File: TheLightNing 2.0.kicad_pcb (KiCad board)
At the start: 2 copper layers, 71 x 51 mm, 26 parts, among them J1 motores izq, J2 motores der, J3 batt, J4 LED_izq, SW1 SW_SPDT, U1 L298(H)N, U2 ESP32_DEVKITC, U3 L7805

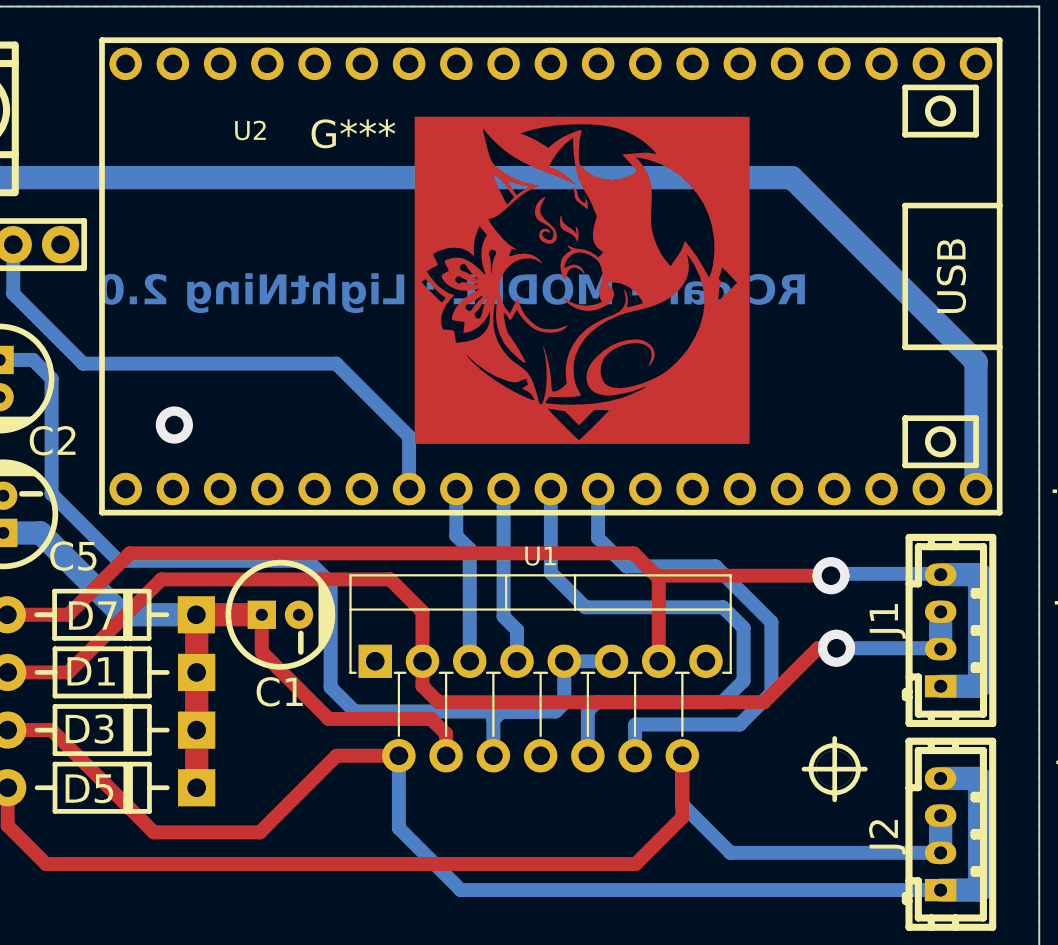
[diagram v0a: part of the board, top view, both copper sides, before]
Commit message: buzzer agregado
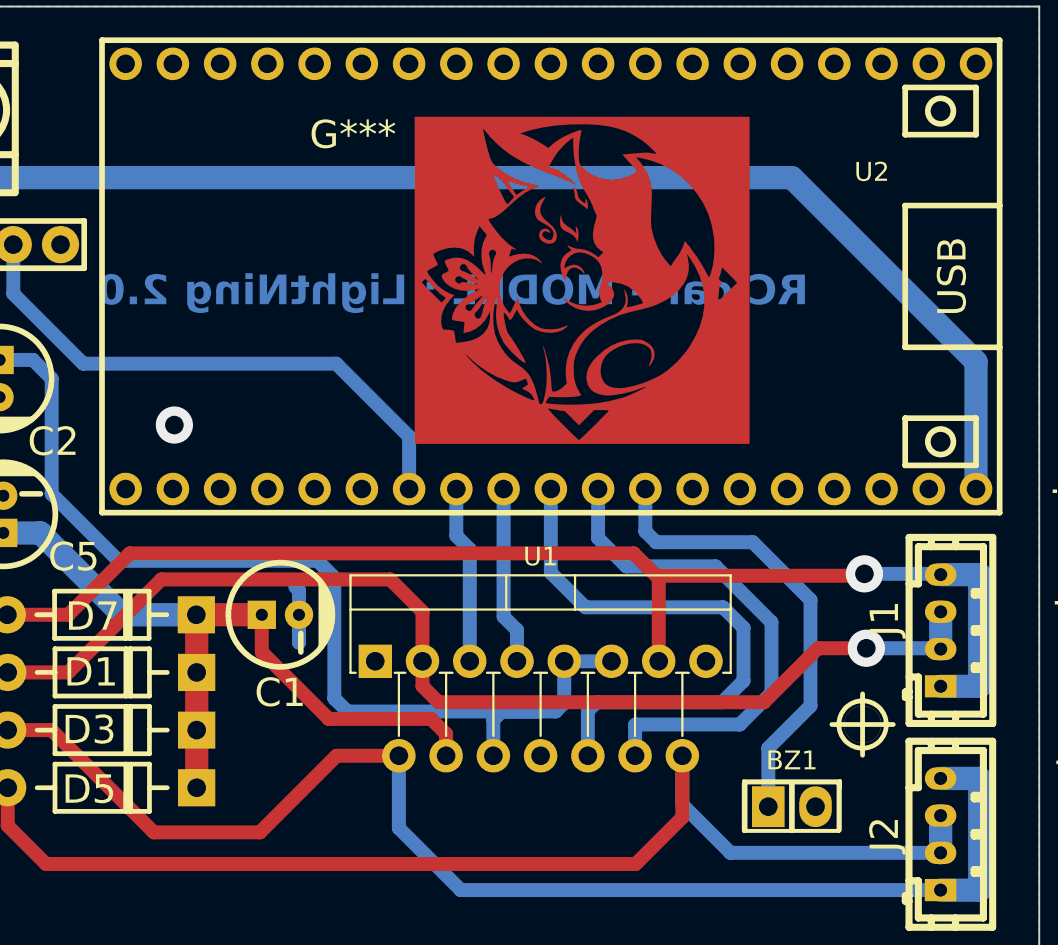
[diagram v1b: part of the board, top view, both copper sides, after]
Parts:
- added BZ1: Buzzer, EESTN5:Pin_Header_2, F.Cu at (92.7, 71.7)
- moved hole_2mm 2.83 mm to (96.5, 67.6)
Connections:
- U2 pad 12: unconnected-(U2-IO14-Pad12) -> /buzz
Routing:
- net /buzz: track 0.00 -> 24.7 mm
- net GND: track 0.00 -> 4.58 mm
- net +5V: track 142.8 -> 143.3 mm

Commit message: re-made
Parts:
- removed G***: LOGO, logo:yae
- removed H1: salida, EESTN5:hole_1mm
- removed the hole_2mm at (96.5, 67.6)
- removed the hole_2mm at (37.0, 77.0)
- removed the hole_2mm at (37.0, 31.0)
- added C6: 100uF 25v, EESTN5:CAP_ELEC_5x11mm, F.Cu at (119.6, 90.4)
- added D9: LED, EESTN5:Pin_strip_2, F.Cu at (120.0, 83.1)
- added J5: dc jack, EESTN5:Pin_Strip_3, F.Cu at (171.1, 97.3)
- added R1: 330, EESTN5:RES0.3, F.Cu at (124.5, 86.9)
- added R2: 22 2W, EESTN5:RES0.3, F.Cu at (127.5, 86.9)
- added U4: L7805, EESTN5:TO-220, F.Cu at (113.8, 88.9)
- added hole_2mm: VAL**, EESTN5:hole_2mm, F.Cu at (187.5, 97.5)
- added hole_2mm: VAL**, EESTN5:hole_2mm, F.Cu at (112.5, 97.5)
- added hole_2mm: VAL**, EESTN5:hole_2mm, F.Cu at (112.5, 42.5)
- moved D4 141.7 mm to (181.3, 42.4), turned to 180 degrees
- moved D6 141.7 mm to (181.3, 45.5), turned to 180 degrees
- moved D8 140.0 mm to (181.3, 48.6), turned to 180 degrees
- moved D2 140.0 mm to (181.3, 51.7), turned to 180 degrees
- moved C1 122.8 mm to (184.9, 89.0)
- moved D3 114.8 mm to (167.6, 42.4), turned to 180 degrees
- moved D5 114.8 mm to (167.6, 45.5), turned to 180 degrees
- moved D7 112.8 mm to (167.6, 48.6), turned to 180 degrees
- moved D1 112.7 mm to (167.6, 51.7), turned to 180 degrees
- moved U1 99.5 mm to (168.5, 80.1), turned to 90 degrees
- moved SW1 82.1 mm to (115.6, 75.0)
- moved J4 80.9 mm to (124.6, 75.0), turned to 90 degrees
- moved J2 77.5 mm to (176.1, 91.2), turned to 0 degrees
- moved J3 76.6 mm to (115.6, 66.5), turned to 90 degrees
- moved C3 75.8 mm to (119.9, 55.6)
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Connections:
- SW1 pad 1: Net-(SW1-A) -> /Cargador
- U2 pad 10: /IN3 -> /IN4
- U2 pad 11: /IN4 -> /IN3
- U2 pad 12: /buzz -> unconnected-(U2-IO14-Pad12)
- U2 pad 30: unconnected-(U2-IO18-Pad30) -> /buzz
- U2 pad 31: unconnected-(U2-IO19-Pad31) -> /led
- U2 pad 7: /led -> unconnected-(U2-IO32-Pad7)
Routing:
- net VCC: track 74.1 -> 172.8 mm
- net Net-(J5-P3): track 0.00 -> 64.7 mm
- net /Cargador: track 0.00 -> 34.5 mm
- net /led: track 29.9 -> 8.98 mm
- net /buzz: track 24.7 -> 4.19 mm
- net +5V: track 143.3 -> 160.7 mm, vias 0 -> 1
- net Net-(U4-OUT): track 0.00 -> 16.7 mm
- net Net-(D1-A): track 64.0 -> 51.1 mm, vias 1 -> 0
- net Net-(SW1-B): track 8.88 -> 17.6 mm
- net /IN3: track 30.4 -> 38.2 mm
- net Net-(D5-A): track 66.6 -> 60.3 mm
- net /IN4: track 27.3 -> 33.3 mm
- net GND: track 4.58 -> 0.00 mm, vias 1 -> 4
- net Net-(SW1-A): track 4.00 -> 0.00 mm
- net Net-(D7-A): track 70.4 -> 66.6 mm, vias 1 -> 0
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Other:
- board size 71 x 51 mm -> 80 x 60 mm
- board text added: "The LightNing 2.0"
- board text removed: "RC car - MODEL : LightNing 2.0"
